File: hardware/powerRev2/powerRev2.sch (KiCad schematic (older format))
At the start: 33 parts

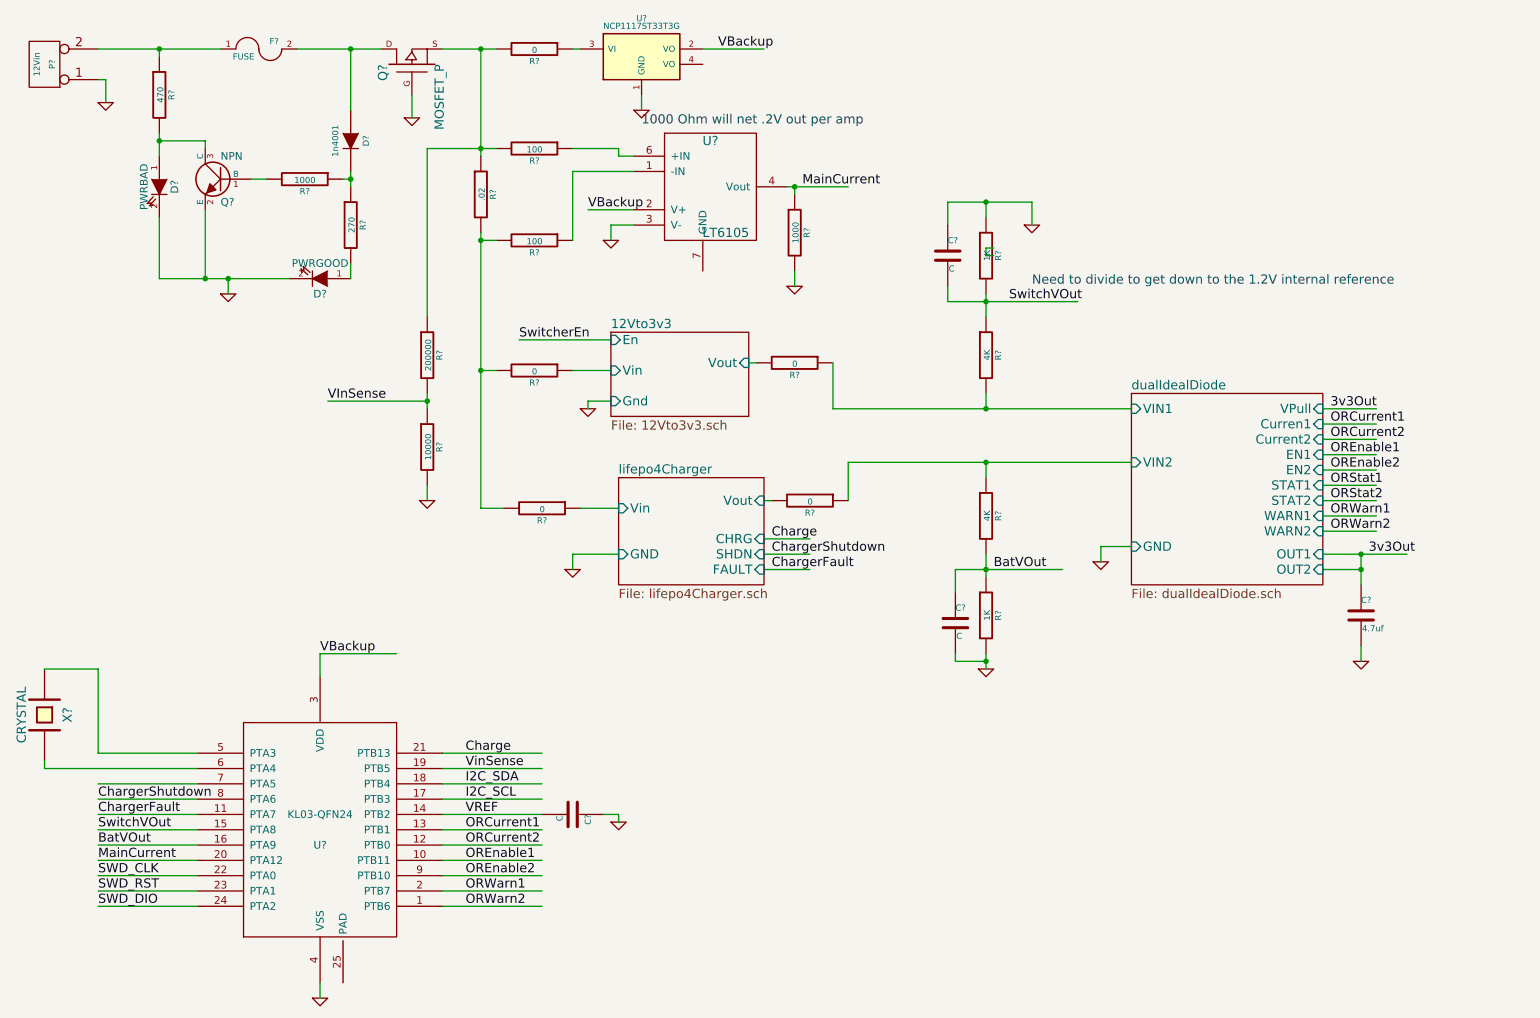
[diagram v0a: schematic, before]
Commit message: More work on the power supply
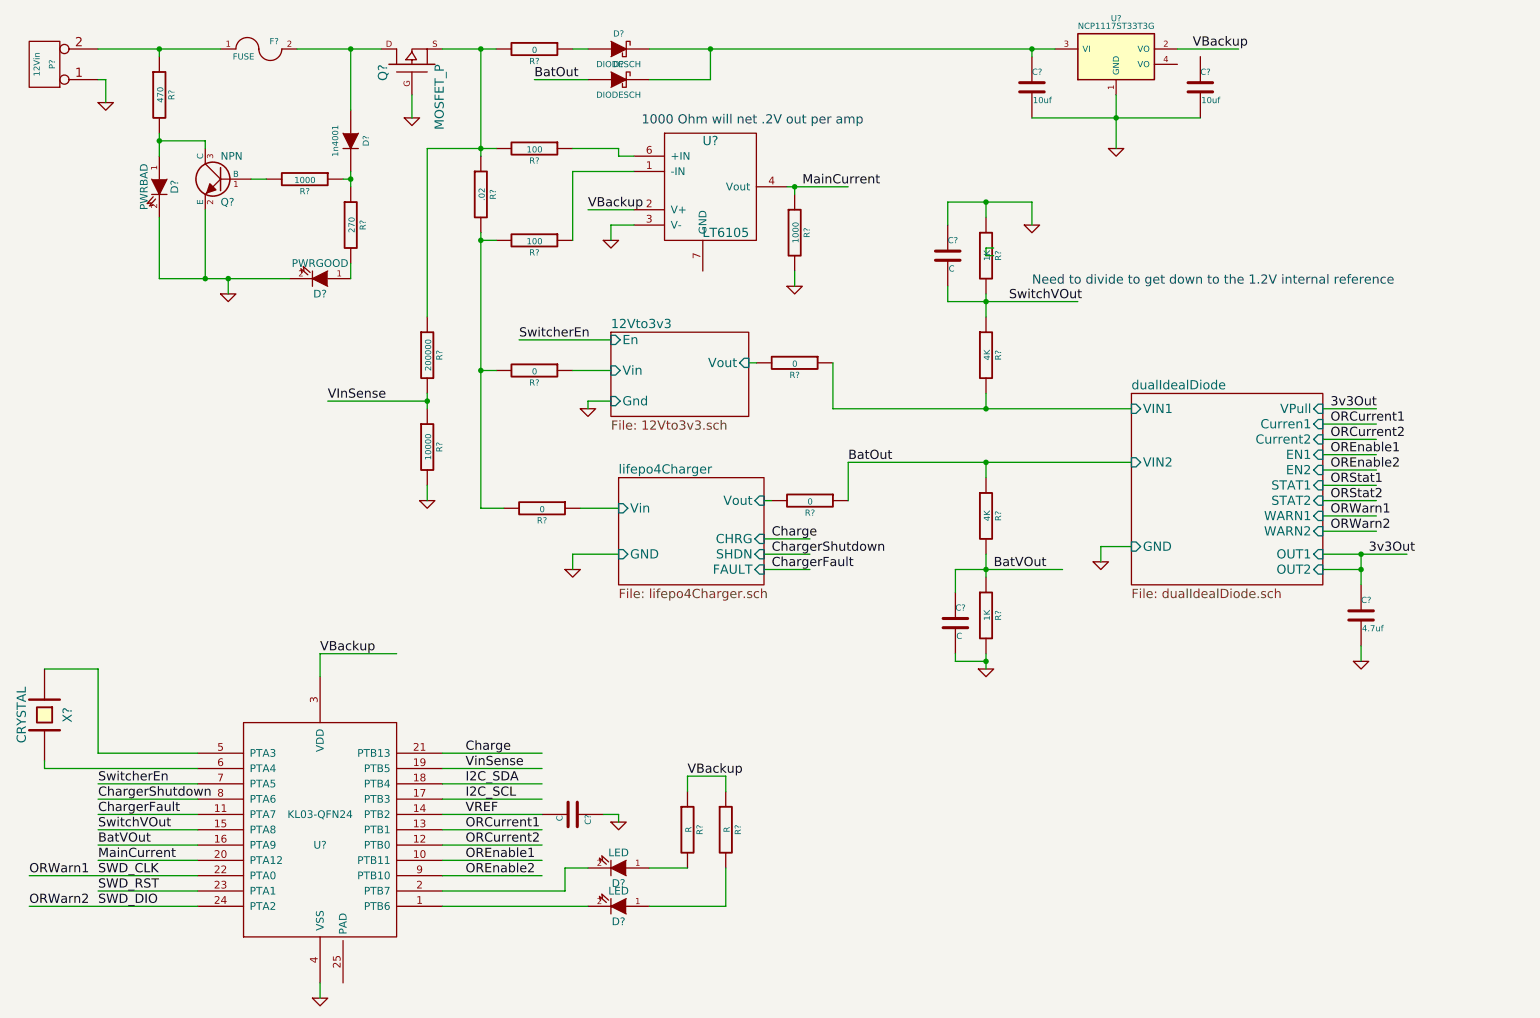
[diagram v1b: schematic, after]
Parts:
- added C? (x2): 10uf, symbol C
- added D? (x2): DIODESCH, symbol DIODESCH
- added D? (x2): LED, symbol LED
- added R? (x2): R, symbol R
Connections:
- net labels added: BatOut
- wire segments 122 -> 136
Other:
- moved on the sheet: U?
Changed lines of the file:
@@
 L NCP1117ST33T3G U?
 U 1 1 561EB20E
-P 4600 800
-F 0 "U?" H 4600 1050 40  0000 C CNN
-F 1 "NCP1117ST33T3G" H 4600 1000 40  0000 C CNN
-F 2 "" H 4600 800 60  0000 C CNN
-F 3 "" H 4600 800 60  0000 C CNN
-	1    4600 800
+P 7700 800
+F 0 "U?" H 7700 1050 40  0000 C CNN
+F 1 "NCP1117ST33T3G" H 7700 1000 40  0000 C CNN
+F 2 "" H 7700 800 60  0000 C CNN
+F 3 "" H 7700 800 60  0000 C CNN
+	1    7700 800
 	1    0    0    -1
 $EndComp
@@
 L GND #PWR?
 U 1 1 561EBA89
-P 4600 1150
-F 0 "#PWR?" H 4600 1150 30  0001 C CNN
-F 1 "GND" H 4600 1080 30  0001 C CNN
-F 2 "" H 4600 1150 60  0000 C CNN
-F 3 "" H 4600 1150 60  0000 C CNN
-	1    4600 1150
+P 7700 1400
+F 0 "#PWR?" H 7700 1400 30  0001 C CNN
+F 1 "GND" H 7700 1330 30  0001 C CNN
+F 2 "" H 7700 1400 60  0000 C CNN
+F 3 "" H 7700 1400 60  0000 C CNN
+	1    7700 1400
 	1    0    0    -1
 $EndComp
 Connection ~ 3550 750
 Wire Wire Line
-	4600 1050 4600 1150
-Wire Wire Line
-	5000 750  5400 750
-Text Label 5100 750  0    60   ~ 0
+	7700 1050 7700 1400
+Wire Wire Line
+	8100 750  8500 750
+Text Label 8200 750  0    60   ~ 0
 VBackup
 Text Label 4250 1800 0    60   ~ 0
@@
 	3300 750  3650 750
 Wire Wire Line
-	4150 750  4200 750
+	4650 750  7300 750
 Wire Wire Line
 	2500 4850 2500 4700
@@
 	1700 6050 1050 6050
 Wire Wire Line
-	1700 6150 1050 6150
+	600  6150 1700 6150
 Wire Wire Line
 	1700 6250 1050 6250
 Wire Wire Line
-	1700 6350 1050 6350
+	600  6350 1700 6350
 Wire Wire Line
 	3300 5350 3950 5350
@@
 	3300 6150 3950 6150
 Wire Wire Line
-	3300 6250 3950 6250
-Wire Wire Line
-	3300 6350 3950 6350
+	3300 6250 4100 6250
+Wire Wire Line
+	3300 6350 4250 6350
 Text Label 1050 6350 0    60   ~ 0
 SWD_DIO
@@
 Text Label 3450 5450 0    60   ~ 0
 VinSense
-Text Label 3450 6250 0    60   ~ 0
-ORWarn1
-Text Label 3450 6350 0    60   ~ 0
-ORWarn2
 $Comp
 L CRYSTAL X?
@@
 Text Label 1050 5650 0    60   ~ 0
 ChargerShutdown
+Text Label 5950 3450 0    60   ~ 0
+BatOut
+$Comp
+L DIODESCH D?
+U 1 1 561EA878
+P 4450 750
+F 0 "D?" H 4450 850 40  0000 C CNN
+F 1 "DIODESCH" H 4450 650 40  0000 C CNN
+F 2 "" H 4450 750 60  0000 C CNN
+F 3 "" H 4450 750 60  0000 C CNN
+	1    4450 750
+	1    0    0    -1
+$EndComp
+$Comp
+L DIODESCH D?
+U 1 1 561EA8FF
+P 4450 950
+F 0 "D?" H 4450 1050 40  0000 C CNN
+F 1 "DIODESCH" H 4450 850 40  0000 C CNN
+F 2 "" H 4450 950 60  0000 C CNN
+F 3 "" H 4450 950 60  0000 C CNN
+	1    4450 950
+	1    0    0    -1
+$EndComp
+Wire Wire Line
+	4250 950  3900 950
+Text Label 3900 950  0    60   ~ 0
+BatOut
+Wire Wire Line
+	4150 750  4250 750
+Wire Wire Line
+	4650 950  5050 950
+Wire Wire Line
+	5050 950  5050 750
+Connection ~ 5050 750
+$Comp
+L C C?
+U 1 1 561EAF4E
+P 7150 1000
+F 0 "C?" H 7150 1100 40  0000 L CNN
+F 1 "10uf" H 7156 915 40  0000 L CNN
+F 2 "" H 7188 850 30  0000 C CNN
+F 3 "" H 7150 1000 60  0000 C CNN
+	1    7150 1000
+	1    0    0    -1
+$EndComp
+$Comp
+L C C?
+U 1 1 561EB17F
+P 8250 1000
+F 0 "C?" H 8250 1100 40  0000 L CNN
+F 1 "10uf" H 8256 915 40  0000 L CNN
+F 2 "" H 8288 850 30  0000 C CNN
+F 3 "" H 8250 1000 60  0000 C CNN
+	1    8250 1000
+	1    0    0    -1
+$EndComp
+Wire Wire Line
+	7150 800  7150 750
+Connection ~ 7150 750
+Wire Wire Line
+	7150 1200 8250 1200
+Connection ~ 7700 1200
+Text Label 600  6150 0    60   ~ 0
+ORWarn1
+Text Label 600  6350 0    60   ~ 0
+ORWarn2
+Text Label 1050 5550 0    60   ~ 0
+SwitcherEn
+$Comp
+L LED D?
+U 1 1 561EC969
+P 4450 6100
+F 0 "D?" H 4450 6200 50  0000 C CNN
+F 1 "LED" H 4450 6000 50  0000 C CNN
+F 2 "" H 4450 6100 60  0000 C CNN
+F 3 "" H 4450 6100 60  0000 C CNN
+	1    4450 6100
+	-1   0    0    1
+$EndComp
+$Comp
+L LED D?
+U 1 1 561ECA36
+P 4450 6350
+F 0 "D?" H 4450 6450 50  0000 C CNN
+F 1 "LED" H 4450 6250 50  0000 C CNN
+F 2 "" H 4450 6350 60  0000 C CNN
+F 3 "" H 4450 6350 60  0000 C CNN
+	1    4450 6350
+	-1   0    0    1
+$EndComp
+$Comp
+L R R?
+U 1 1 561ECAC6
+P 4900 5850
+F 0 "R?" V 4980 5850 40  0000 C CNN
+F 1 "R" V 4907 5851 40  0000 C CNN
+F 2 "" V 4830 5850 30  0000 C CNN
+F 3 "" H 4900 5850 30  0000 C CNN
+	1    4900 5850
+	1    0    0    -1
+$EndComp
+$Comp
+L R R?
+U 1 1 561ECB63
+P 5150 5850
+F 0 "R?" V 5230 5850 40  0000 C CNN
+F 1 "R" V 5157 5851 40  0000 C CNN
+F 2 "" V 5080 5850 30  0000 C CNN
+F 3 "" H 5150 5850 30  0000 C CNN
+	1    5150 5850
+	1    0    0    -1
+$EndComp
+Wire Wire Line
+	4250 6100 4100 6100
+Wire Wire Line
+	4100 6100 4100 6250
+Wire Wire Line
+	5150 6100 5150 6350
+Wire Wire Line
+	5150 6350 4650 6350
+Wire Wire Line
+	4650 6100 4900 6100
+Wire Wire Line
+	4900 5600 4900 5500
+Wire Wire Line
+	4900 5500 5150 5500
+Wire Wire Line
+	5150 5500 5150 5600
+Text Label 4900 5500 0    60   ~ 0
+VBackup
 $EndSCHEMATC
